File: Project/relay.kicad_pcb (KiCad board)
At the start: 2 copper layers, 23.4 x 22.4 mm, 11 parts

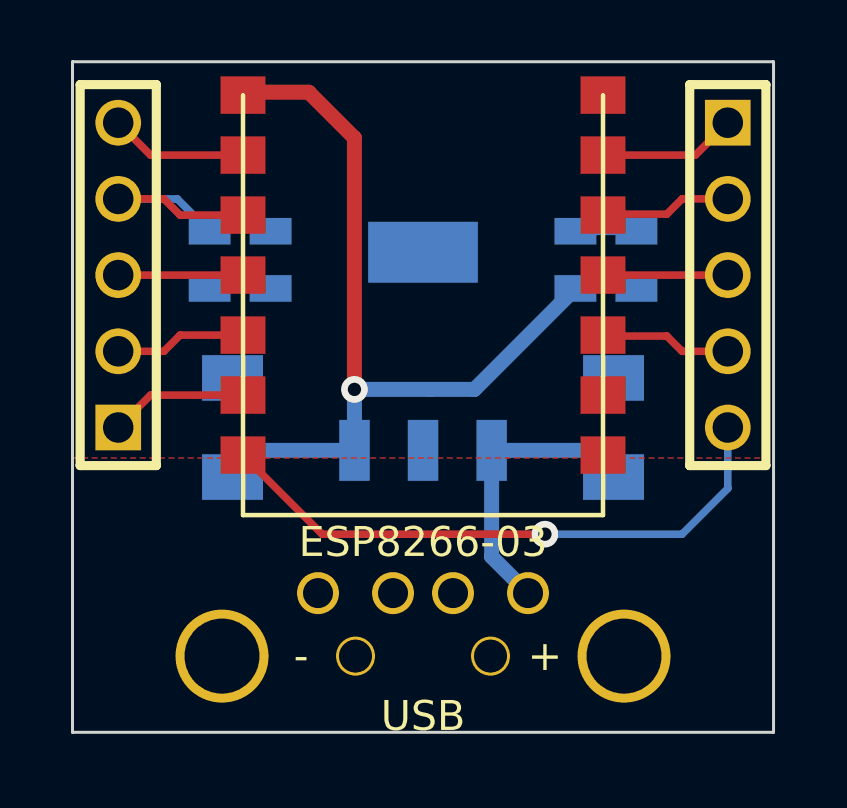
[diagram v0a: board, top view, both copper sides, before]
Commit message: Lots of enhancements to PCB
Added pins for VCC and GND, downsized PCB footprint, Added solder
jumpers to permanently pull up/down various pins.
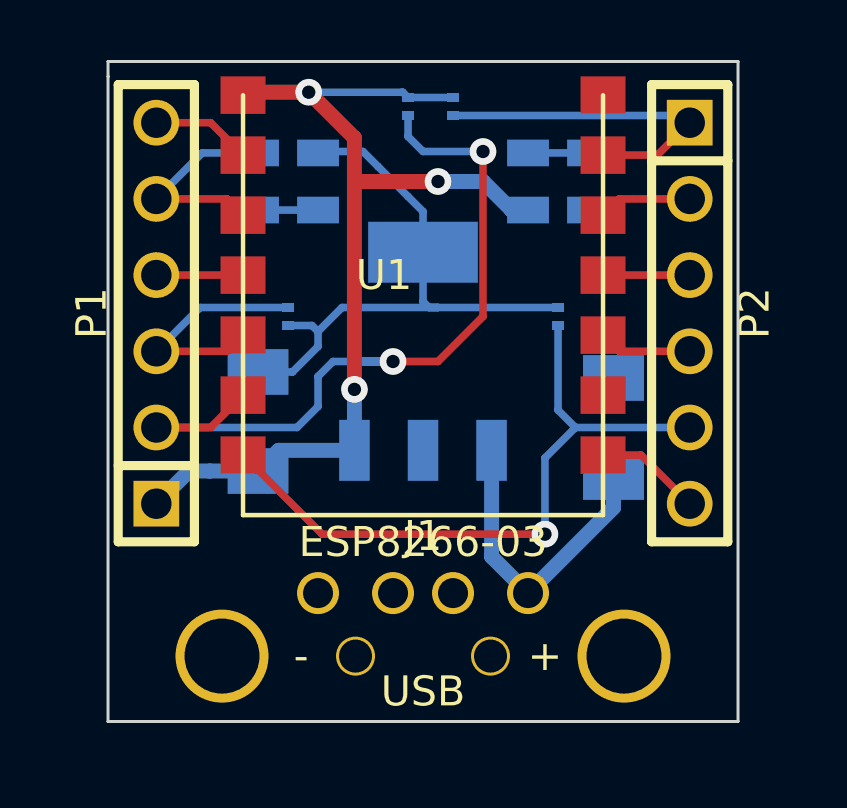
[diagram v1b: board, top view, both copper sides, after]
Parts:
- removed ? (x2): CONN_5, PIN_ARRAY_5x1
- added P1: CONN_6, PIN_ARRAY-6X1, F.Cu at (181.6, 135.9)
- added P2: CONN_6, PIN_ARRAY-6X1, F.Cu at (199.4, 135.9)
- added R3: J, SM0201_r, B.Cu at (186.0, 136.0)
- added R4: J, SM0201_r, B.Cu at (190.0, 129.0)
- added R5: J, SM0201_r, B.Cu at (195.0, 136.0)
- added R6: J, SM0201_r, B.Cu at (191.5, 129.0)
- moved D2 3.07 mm to (196.0, 131.5)
- moved R1 3.07 mm to (185.0, 131.5)
- moved D1 3.05 mm to (187.0, 131.5)
- moved R2 3.05 mm to (194.0, 131.5)
- moved C2 0.87 mm to (185.0, 139.5)
- gave numbers to parts that had none: 2
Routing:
- net N-0000012: track 4.61 -> 31.3 mm, vias 0 -> 2
- net GND: track 0.00 -> 23.8 mm
- net N-0000014: track 4.61 -> 11.3 mm
- net VCC: track 28.0 -> 33.2 mm, vias 1 -> 3
- net N-000003: track 4.38 -> 8.11 mm
- net N-0000010: track 19.9 -> 22.6 mm
- net N-000002: track 4.61 -> 3.34 mm
- net N-000006: track 4.16 -> 2.89 mm
- net N-000004: track 4.16 -> 2.89 mm
- net N-000008: track 4.38 -> 3.11 mm
- net N-000007: track 4.38 -> 3.11 mm
- net N-000005: track 7.88 -> 7.14 mm
- net N-0000019: track 9.69 -> 10.3 mm
- removed copper zone on F.Cu, net GND
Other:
- board size 23.4 x 22.4 mm -> 21 x 22 mm
